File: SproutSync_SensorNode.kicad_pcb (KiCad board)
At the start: 2 copper layers, 32 x 70.2 mm, 81 parts, among them J1 S2B-PH-K-S, J3 OSTVN04A150, J4 10132797-031100LF, J5 10132797-031100LF, J6 OSTVN02A150, J7 Conn_01x03, Q1 PMH950UPEH, Q2 AS2302, Q3 SIUD412ED-T1-GE3, Q5 SIUD412ED-T1-GE3, Q6 SIUD412ED-T1-GE3, U1 LTR-329ALS-01, U4 SN65HVD3082EDR, U5 TXB0104RGYR, U6 TPS629203DRL, U7 BME688, U9 TPS629206DRLR

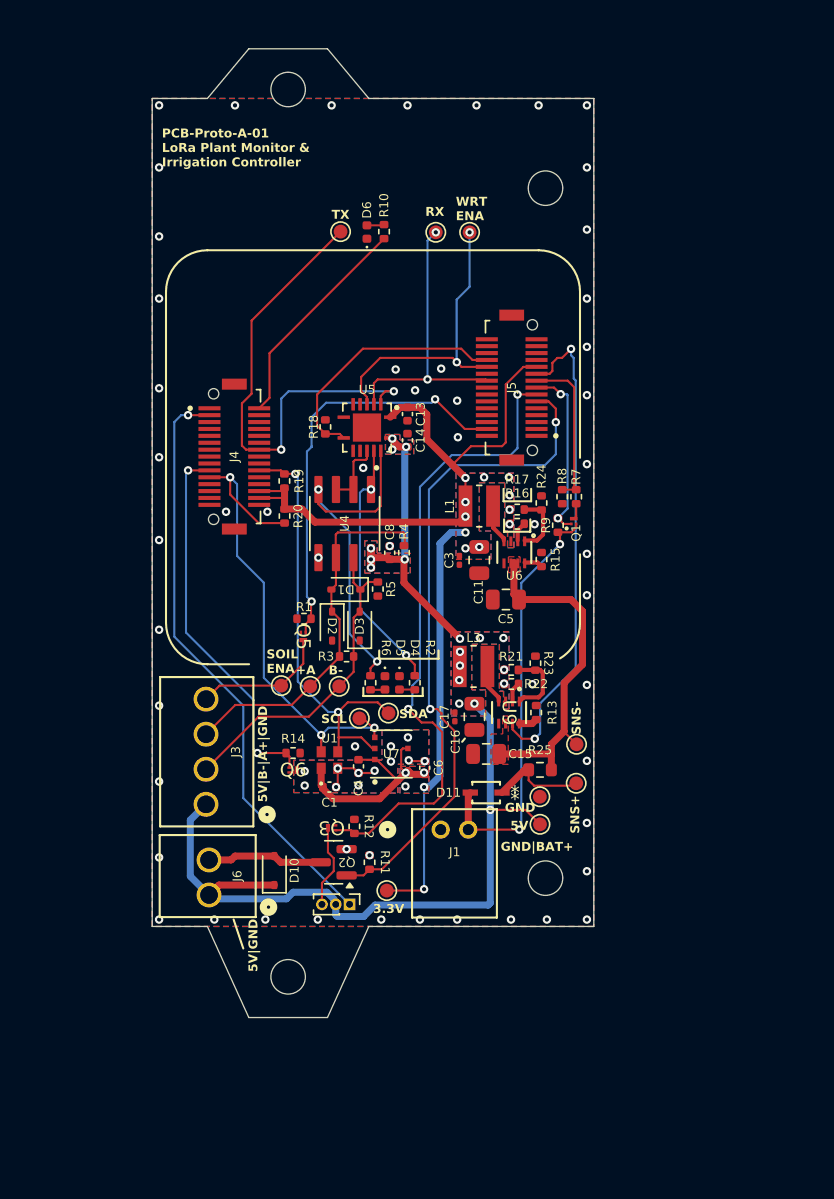
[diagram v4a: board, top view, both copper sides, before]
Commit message: Removed via in pads
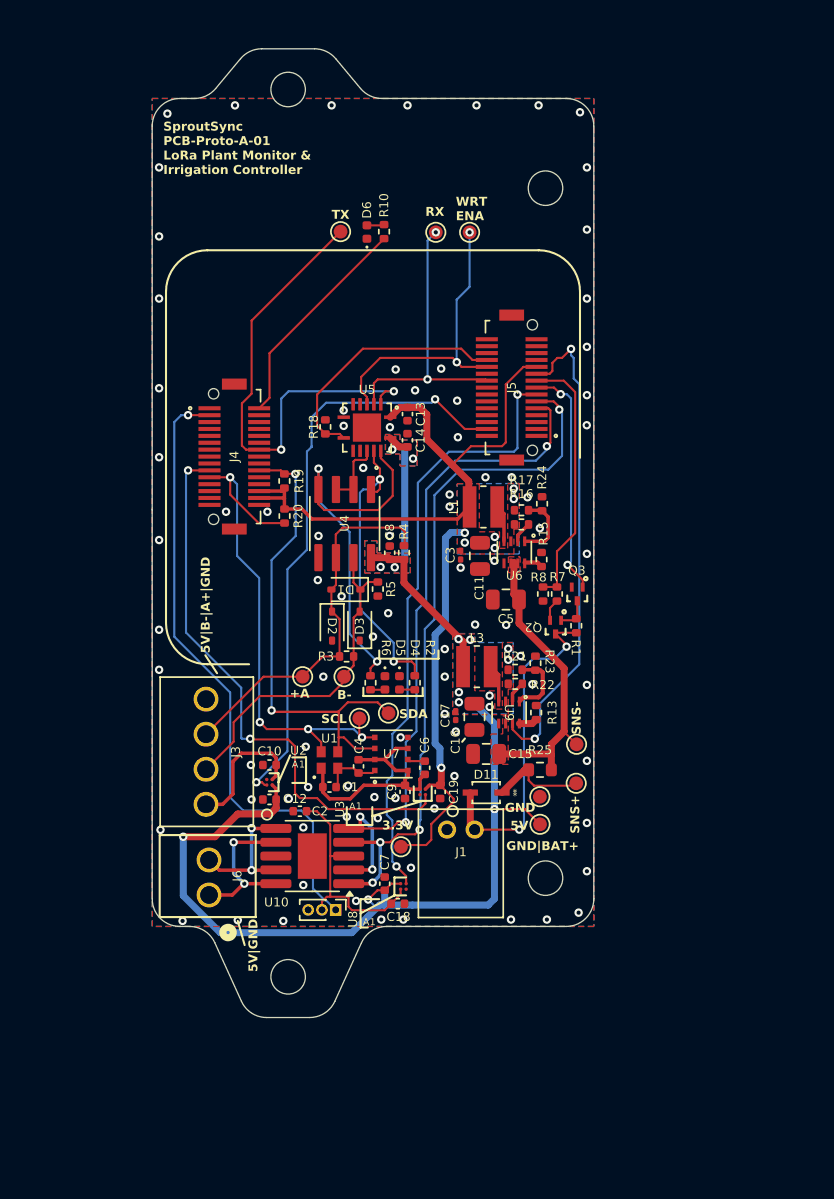
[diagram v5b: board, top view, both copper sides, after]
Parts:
- removed D10: 1N4148WS, Diode_SMD:D_SOD-323
- removed Q1: PMH950UPEH, SproutSenseFootprints:QPMOS1G2S3d_SOT8001_NEX
- removed Q5, Q6: SIUD412ED-T1-GE3, SproutSenseFootprints:SMT_412ED-T1-GE3_VIS
- removed R11: 22k, Resistor_SMD:R_0402_1005Metric
- removed R12, R14, R9: 4.7k, Resistor_SMD:R_0402_1005Metric
- removed TP5: TestPoint, TestPoint:TestPoint_Pad_D1.0mm
- added C10: 1uF, Capacitor_SMD:C_0402_1005Metric, F.Cu at (97.5, 112.3)
- added C12: 22uF, Capacitor_SMD:C_0402_1005Metric, F.Cu at (97.5, 114.8)
- added C18: 1uF, Capacitor_SMD:C_0402_1005Metric, F.Cu at (106.8, 122.3)
- added C19: 22uF, Capacitor_SMD:C_0402_1005Metric, F.Cu at (109.9, 114.2)
- added C2: 22uF, Capacitor_SMD:C_0402_1005Metric, F.Cu at (99.7, 115.7)
- added C7: 22uF, Capacitor_SMD:C_0402_1005Metric, F.Cu at (105.8, 120.9)
- added C9: 1uF, Capacitor_SMD:C_0402_1005Metric, F.Cu at (107.3, 114.2)
- added U10: A3909GLNTR-T, SproutSenseFootprints:SSOP-10-1EP_3.9x4.9mm_P1mm_EP2.1x3.3mm, F.Cu at (100.6, 118.9)
- added U2: TPS22914BYFPR, SproutSenseFootprints:YFP4_TEX, F.Cu at (97.5, 113.5)
- added U3: TPS22914BYFPR, SproutSenseFootprints:YFP4_TEX, F.Cu at (108.6, 114.2)
- added U8: TPS22914BYFPR, SproutSenseFootprints:YFP4_TEX, F.Cu at (107.2, 121.1)
- Q2: value AS2302 -> SSM3J35MFV; footprint Package_TO_SOT_SMD:SOT-23 -> SproutSenseFootprints:VESM_TOS
- Q3: value SIUD412ED-T1-GE3 -> SSM3K16FV; footprint SproutSenseFootprints:SMT_412ED-T1-GE3_VIS -> SproutSenseFootprints:VESM_TOS
- R1: value 4.7k -> 47k
- moved Q3 24.6 mm to (119.8, 99.9)
- moved Q2 23.4 mm to (118.2, 102.3)
- moved R1 19.7 mm to (119.7, 102.2), turned to -90 degrees
- moved R7 7.19 mm to (118.3, 99.9)
- moved R8 7.19 mm to (117.3, 99.9)
- moved TP14 3.34 mm to (107.0, 118.2)
- moved J7 1.08 mm to (102.3, 122.8)
- moved TP4 0.89 mm to (99.9, 105.9)
- moved TP3 0.78 mm to (102.9, 105.9)
- moved J1 0.46 mm to (110.4, 117.0)
- moved C3 0.39 mm to (111.3, 97.1)
- moved R16 0.31 mm to (115.8, 94.9)
- moved R17 0.31 mm to (115.8, 93.8)
- moved L1 0.31 mm to (113.0, 93.6)
- moved C11 0.30 mm to (112.8, 97.2)
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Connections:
- C1 pad 1: +3V3 -> AMB_PWR_3p3
- C1 pad 2: AMB_LOW_SW -> GND
- C4 pad 1: +3V3 -> AMB_PWR_3p3
- C4 pad 2: AMB_LOW_SW -> GND
- C6 pad 1: +3V3 -> AMB_PWR_3p3
- C6 pad 2: AMB_LOW_SW -> GND
- J3 pad 1: +5V -> SOIL_PWR_5p0
- J3 pad 4: Net-(J3-Pin_4) -> GND
- J6 pad 1: +5V -> Net-(J6-Pin_1)
- J6 pad 2: Net-(D10-A) -> Net-(J6-Pin_2)
- J7 pad 2: +5V -> IRRI_PWR_5p0
- J7 pad 3: Net-(J7-Pin_3) -> GND
- Q2 pad 1: /PetalStackingConectors/PAD13 -> Net-(Q2-G)
- Q2 pad 2: GND -> Net-(Q2-S)
- Q2 pad 3: Net-(D10-A) -> /Power/BAT_POS
- Q3 pad 1: /PetalStackingConectors/PAD15 -> /PetalStackingConectors/PAD32
- Q3 pad 3: Net-(J7-Pin_3) -> Net-(Q2-G)
- R1 pad 1: GND -> Net-(Q2-G)
- R1 pad 2: /PetalStackingConectors/PAD29 -> /Power/BAT_POS
- R7 pad 2: Net-(Q1-D) -> Net-(Q2-S)
- U1 pad 1: +3V3 -> AMB_PWR_3p3
- U1 pad 2: AMB_LOW_SW -> GND
- U7 pad 1: AMB_LOW_SW -> GND
- U7 pad 2: +3V3 -> AMB_PWR_3p3
- U7 pad 5: AMB_LOW_SW -> GND
- U7 pad 6: +3V3 -> AMB_PWR_3p3
- U7 pad 7: AMB_LOW_SW -> GND
- U7 pad 8: +3V3 -> AMB_PWR_3p3
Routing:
- net /PetalStackingConectors/PAD12: track 0.00 -> 49.8 mm, vias 0 -> 4
- net +3V3: track 87.8 -> 69.5 mm, vias 16 -> 7
- net AMB_PWR_3p3: track 0.00 -> 17.9 mm
- net IRRI_PWR_5p0: track 0.00 -> 16.8 mm
- net /PetalStackingConectors/PAD7: track 27.5 -> 41.0 mm
- net /PetalStackingConectors/PAD29: track 30.3 -> 43.2 mm
- net Net-(J6-Pin_1): track 0.00 -> 11.6 mm, vias 0 -> 2
- net Net-(J6-Pin_2): track 0.00 -> 10.0 mm, vias 0 -> 2
- net Net-(J3-Pin_4): track 9.82 -> 0.00 mm
- net SOIL_PWR_5p0: track 0.00 -> 9.81 mm
- net +5V: track 74.1 -> 83.3 mm, vias 18 -> 15
- net /PetalStackingConectors/PAD49: track 32.1 -> 40.6 mm
- net Net-(D10-A): track 8.40 -> 0.00 mm
- net /PetalStackingConectors/PAD33: track 11.4 -> 18.8 mm
- net /Power/BAT_POS: track 31.0 -> 24.5 mm
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- removed copper zone on B.Cu, net AMB_LOW_SW
- removed copper zone on F.Cu, net AMB_LOW_SW
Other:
- outline, holes or cut-outs redrawn
- board text added: "SproutSync PCB-Proto-A-01 LoRa Plant Monitor & Irrigation Controller"
- board text removed: "PCB-Proto-A-01 LoRa Plant Monitor & Irrigation Controller"
- board text removed: "SOIL ENA"

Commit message: Swapped H bridge and irrigation conn
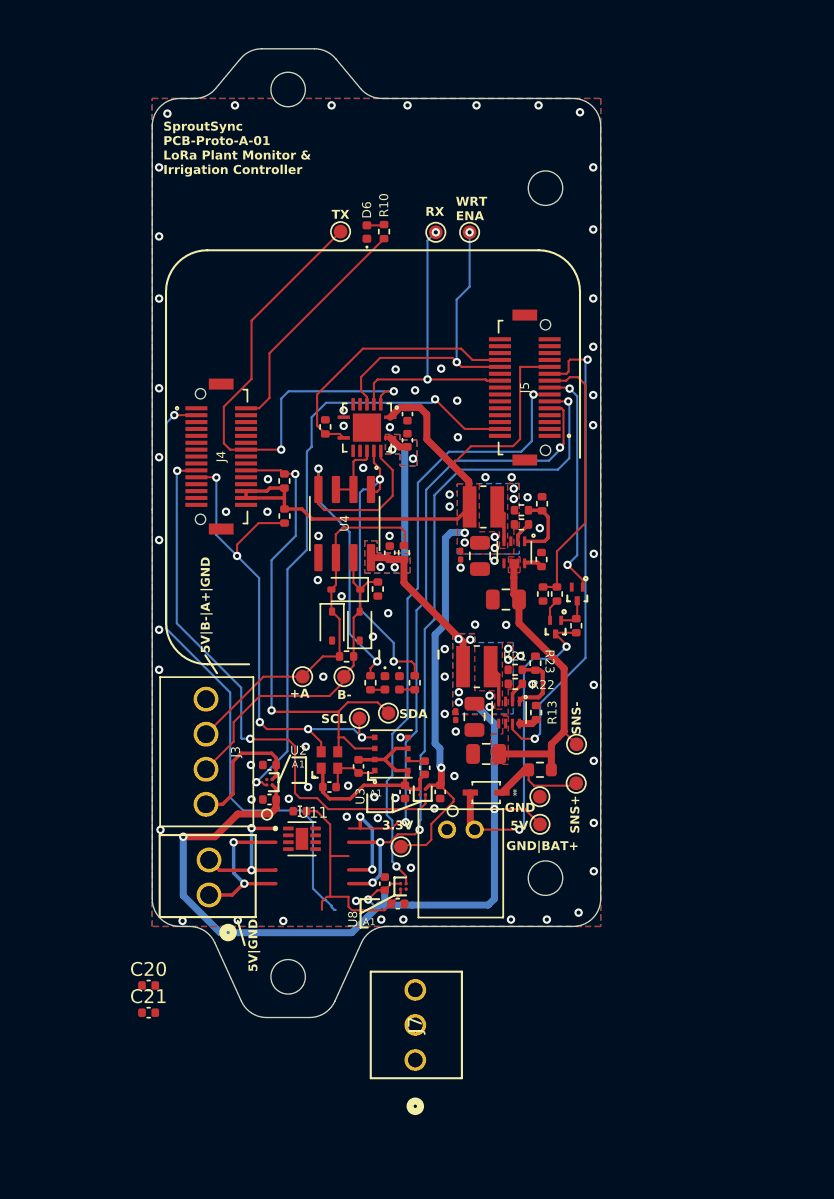
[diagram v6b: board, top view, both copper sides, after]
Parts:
- removed U10: A3909GLNTR-T, SproutSenseFootprints:SSOP-10-1EP_3.9x4.9mm_P1mm_EP2.1x3.3mm
- added C20: 100nF, Capacitor_SMD:C_0402_1005Metric, F.Cu at (88.7, 128.3)
- added C21: 100nF, Capacitor_SMD:C_0402_1005Metric, F.Cu at (88.7, 130.2)
- added U11: DRV8838DSGR, SproutSenseFootprints:SON50P200X200X80-9N, F.Cu at (99.9, 117.7)
- J7: footprint Connector_PinHeader_1.00mm:PinHeader_1x03_P1.00mm_Vertical -> SproutSenseFootprints:CONN_A-6373-03A_MOL
- moved J7 12.3 mm to (108.1, 133.7), turned to 90 degrees
- moved J4 0.95 mm to (94.0, 90.0)
- moved J5 0.95 mm to (116.0, 85.0)
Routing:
- net +3V3: track 69.5 -> 73.4 mm
- net /PetalStackingConectors/PAD30: track 35.2 -> 37.0 mm
- net /PetalStackingConectors/PAD2: track 18.6 -> 19.5 mm
- net /PetalStackingConectors/PAD49: track 40.6 -> 41.6 mm
- net /PetalStackingConectors/PAD31: track 20.8 -> 21.7 mm
- net /PetalStackingConectors/PAD29: track 43.2 -> 44.1 mm
- net /PetalStackingConectors/PAD1: track 21.9 -> 22.9 mm
- net /LEDIndicators/LORA_TX: track 16.0 -> 17.0 mm
- net /PetalStackingConectors/PAD12: track 49.8 -> 50.8 mm
- net /PetalStackingConectors/PAD48: track 38.5 -> 37.7 mm, vias 4 -> 5
- net /PetalStackingConectors/PAD35: track 35.7 -> 35.0 mm
- net /PetalStackingConectors/PAD33: track 18.8 -> 19.4 mm
- net /PetalStackingConectors/PAD15: track 44.2 -> 44.8 mm
- net /PetalStackingConectors/PAD13: track 51.0 -> 51.5 mm
- net GND: vias 86 -> 85
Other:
- board size 32 x 70.2 mm -> 32.5 x 70.2 mm
